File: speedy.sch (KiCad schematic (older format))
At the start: 22 parts

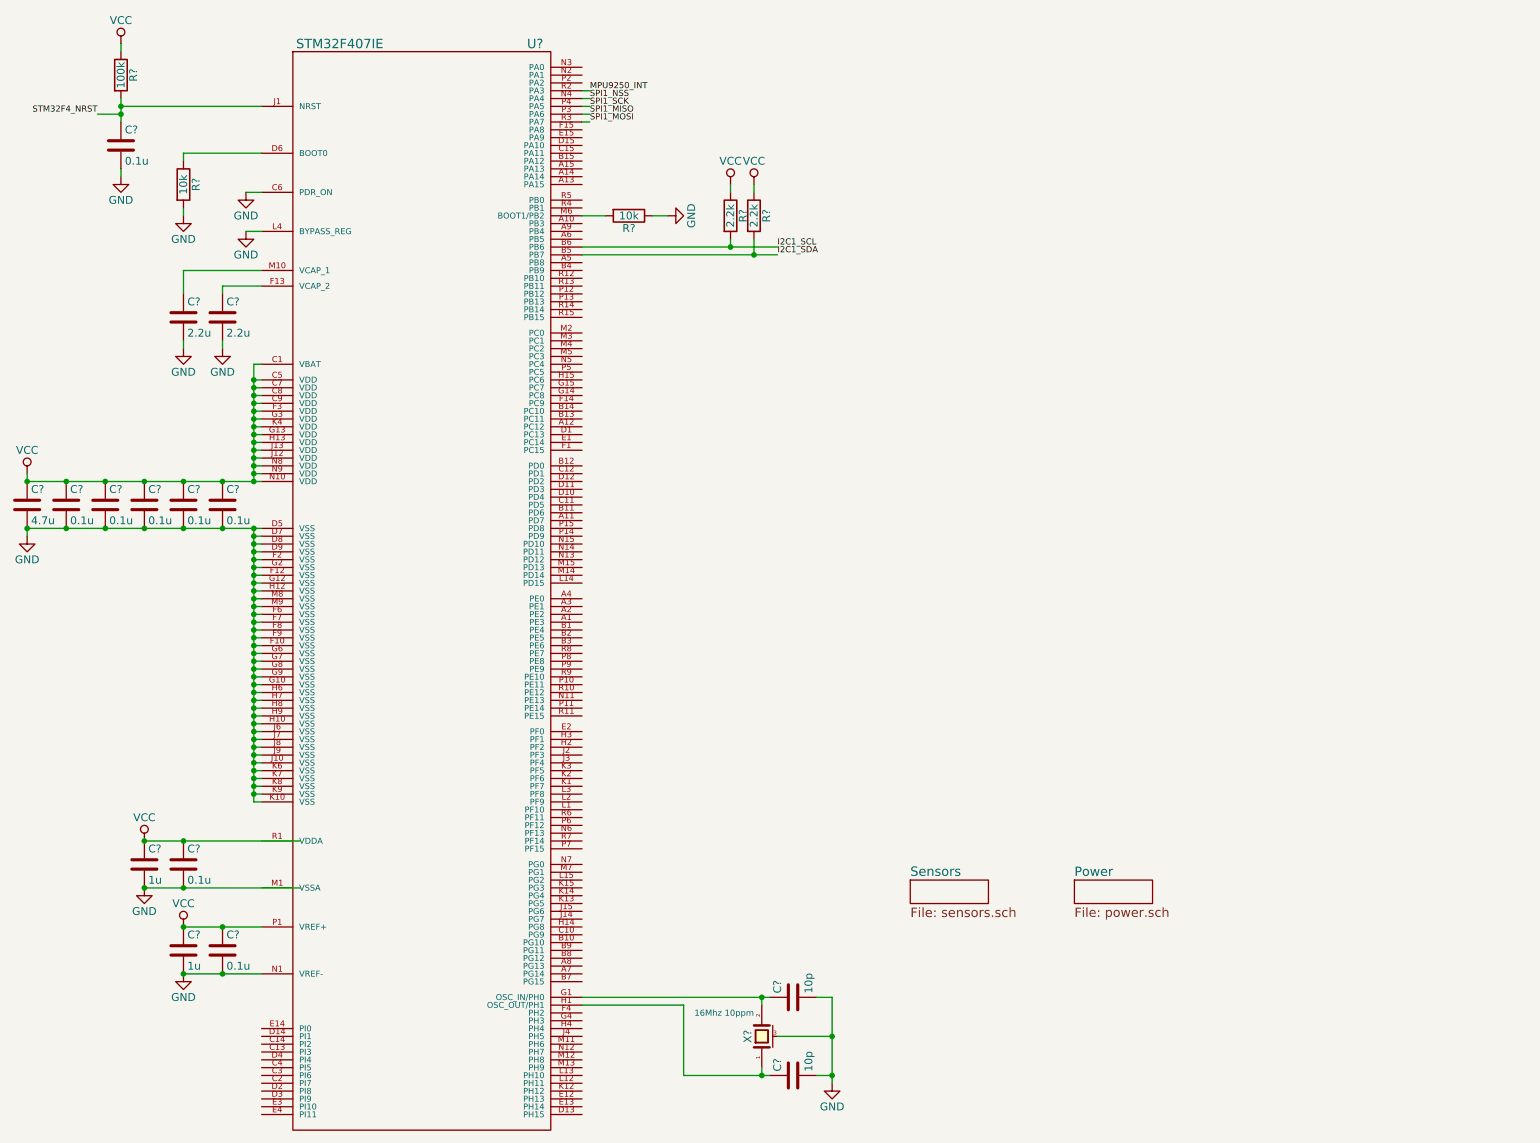
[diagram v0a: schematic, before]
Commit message: LiPo recharge circuit
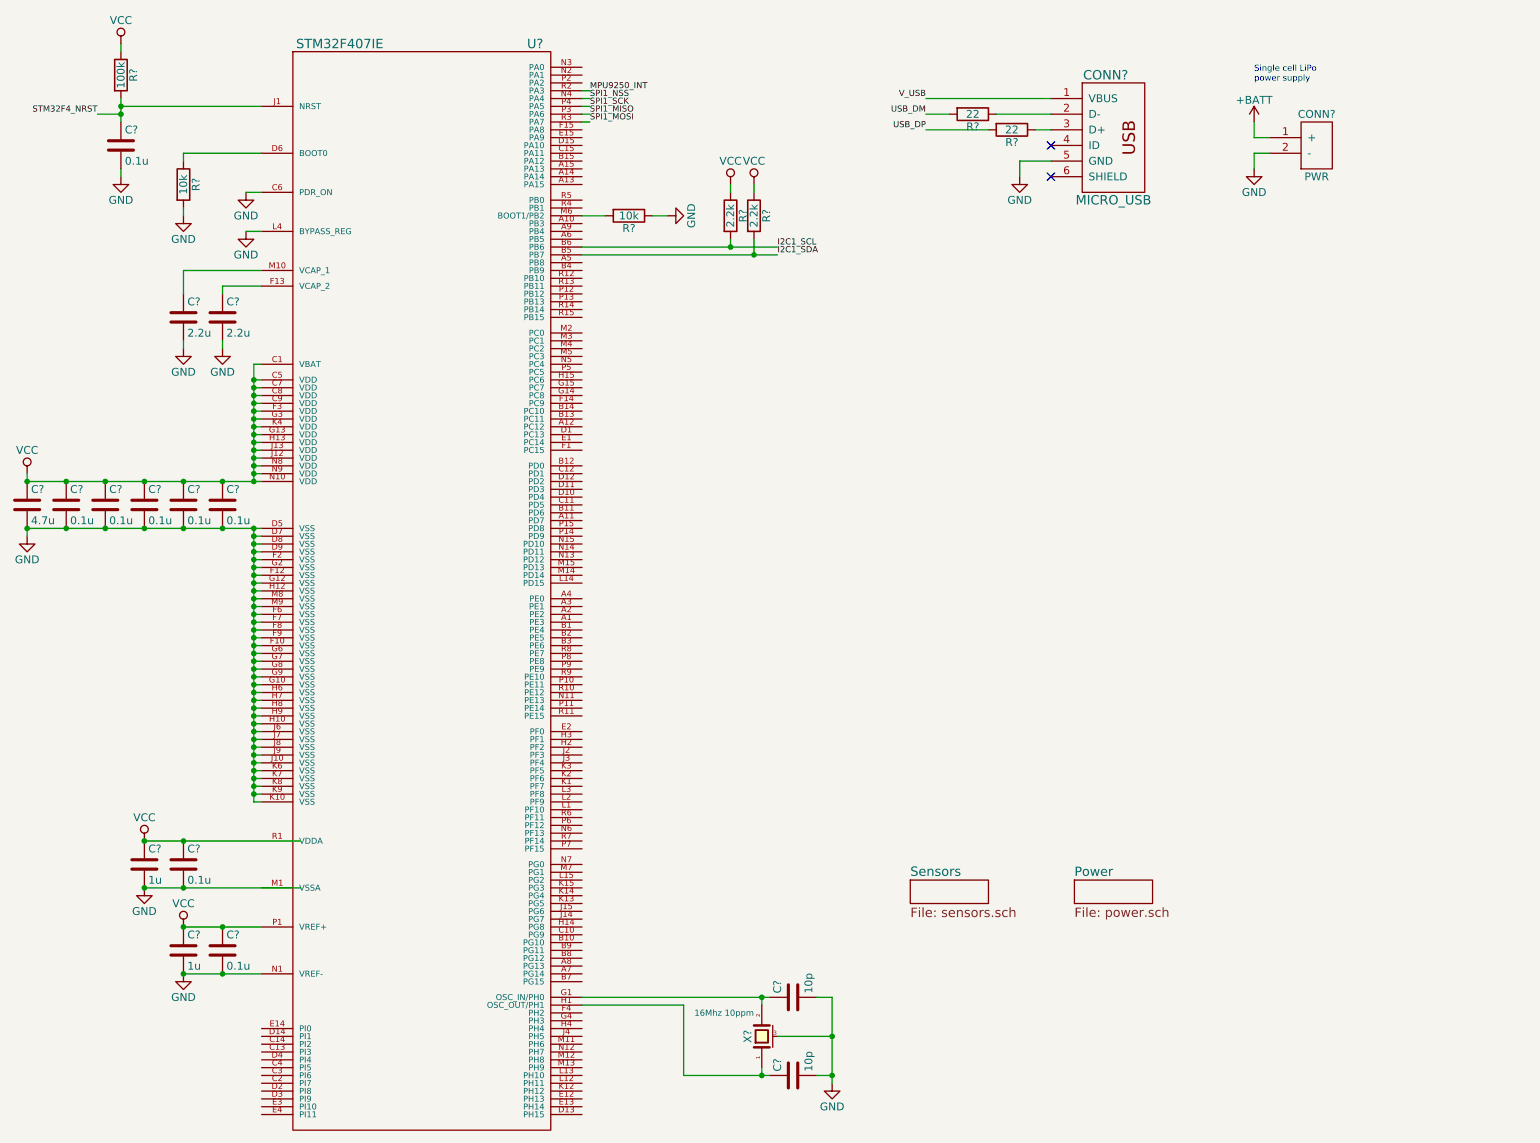
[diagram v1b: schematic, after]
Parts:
- added CONN?: MICRO_USB, symbol MICRO_USB
- added CONN?: PWR, MODULE, symbol PWR
- added R? (x2): 22, symbol R
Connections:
- net GND: now also CONN?.2 (-), CONN?.5 (GND), CONN?.MECH (GND)
- new net: CONN?.2 (D-), R?.1
- new net: CONN?.3 (D+), R?.1
- new net +BATT: CONN?.1 (+)
- new net USB_DM: R?.2
- new net USB_DP: R?.2
- new net V_USB: CONN?.1 (VBUS)
- no-connect marks 0 -> 2
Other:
- note added: "Single cell LiPo \npower supply\n"

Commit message: Update schematic labels to handle hierarchical signal dependencies
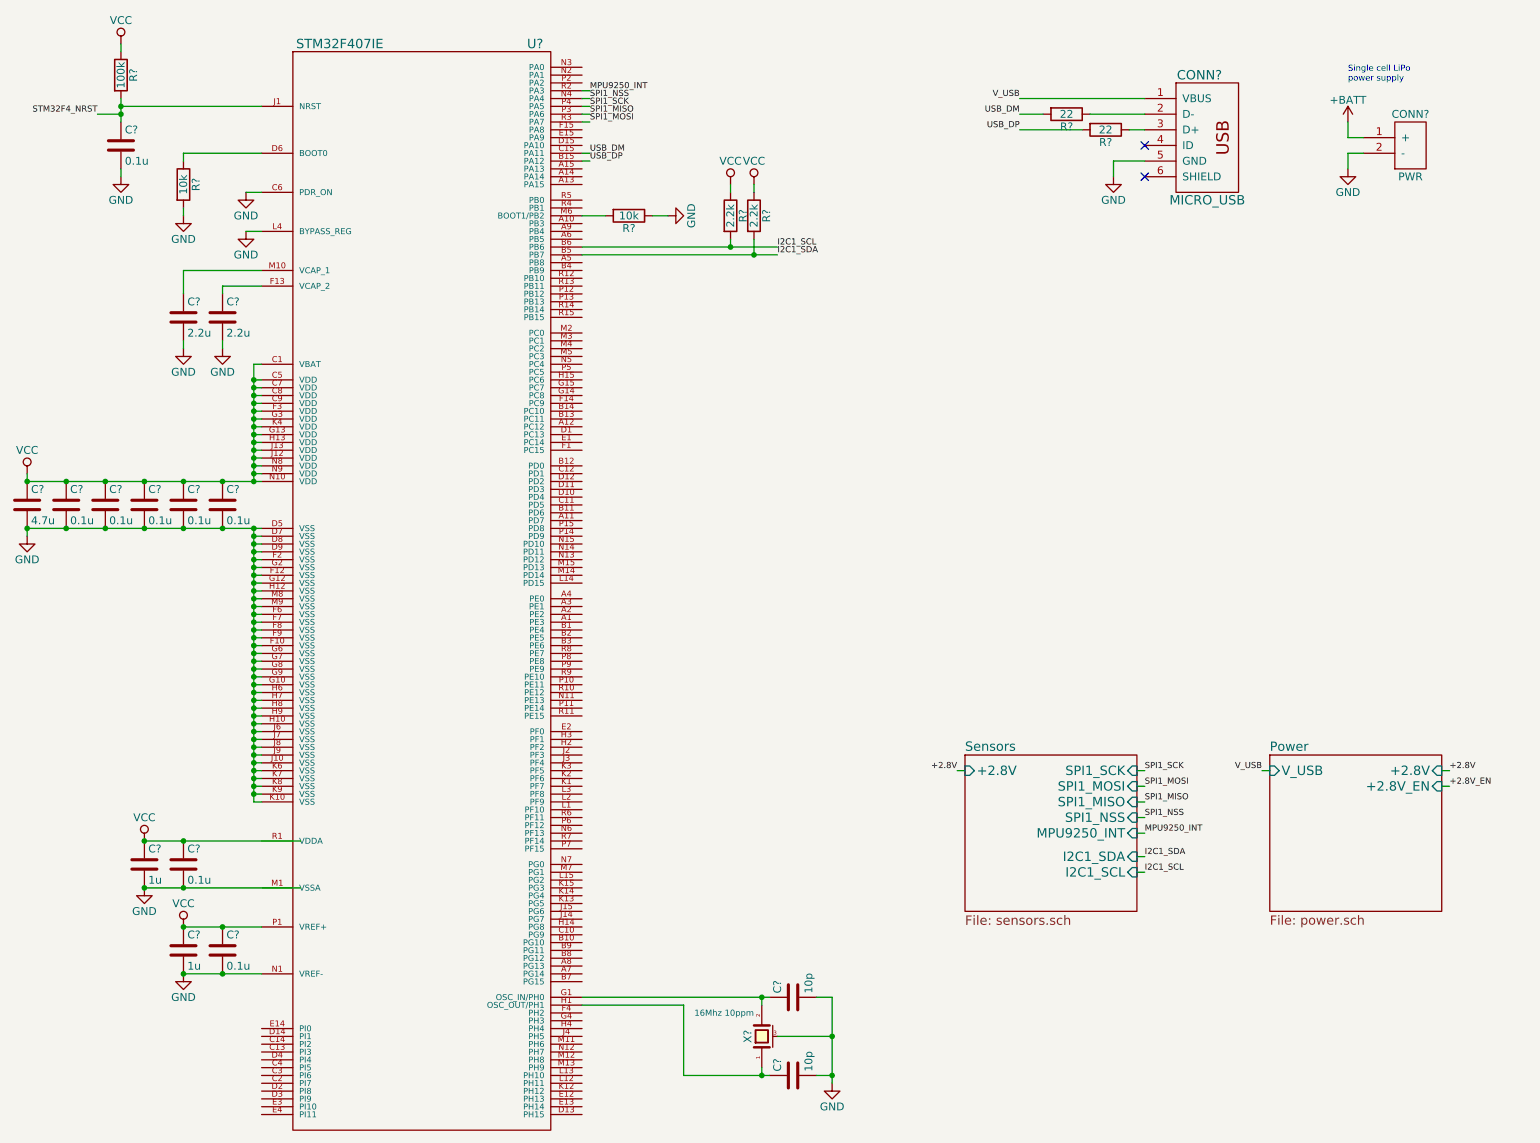
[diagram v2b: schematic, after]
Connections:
- net USB_DM: now also U?.C15 (PA11)
- net USB_DP: now also U?.B15 (PA12)
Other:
- moved on the sheet: CONN?, R?

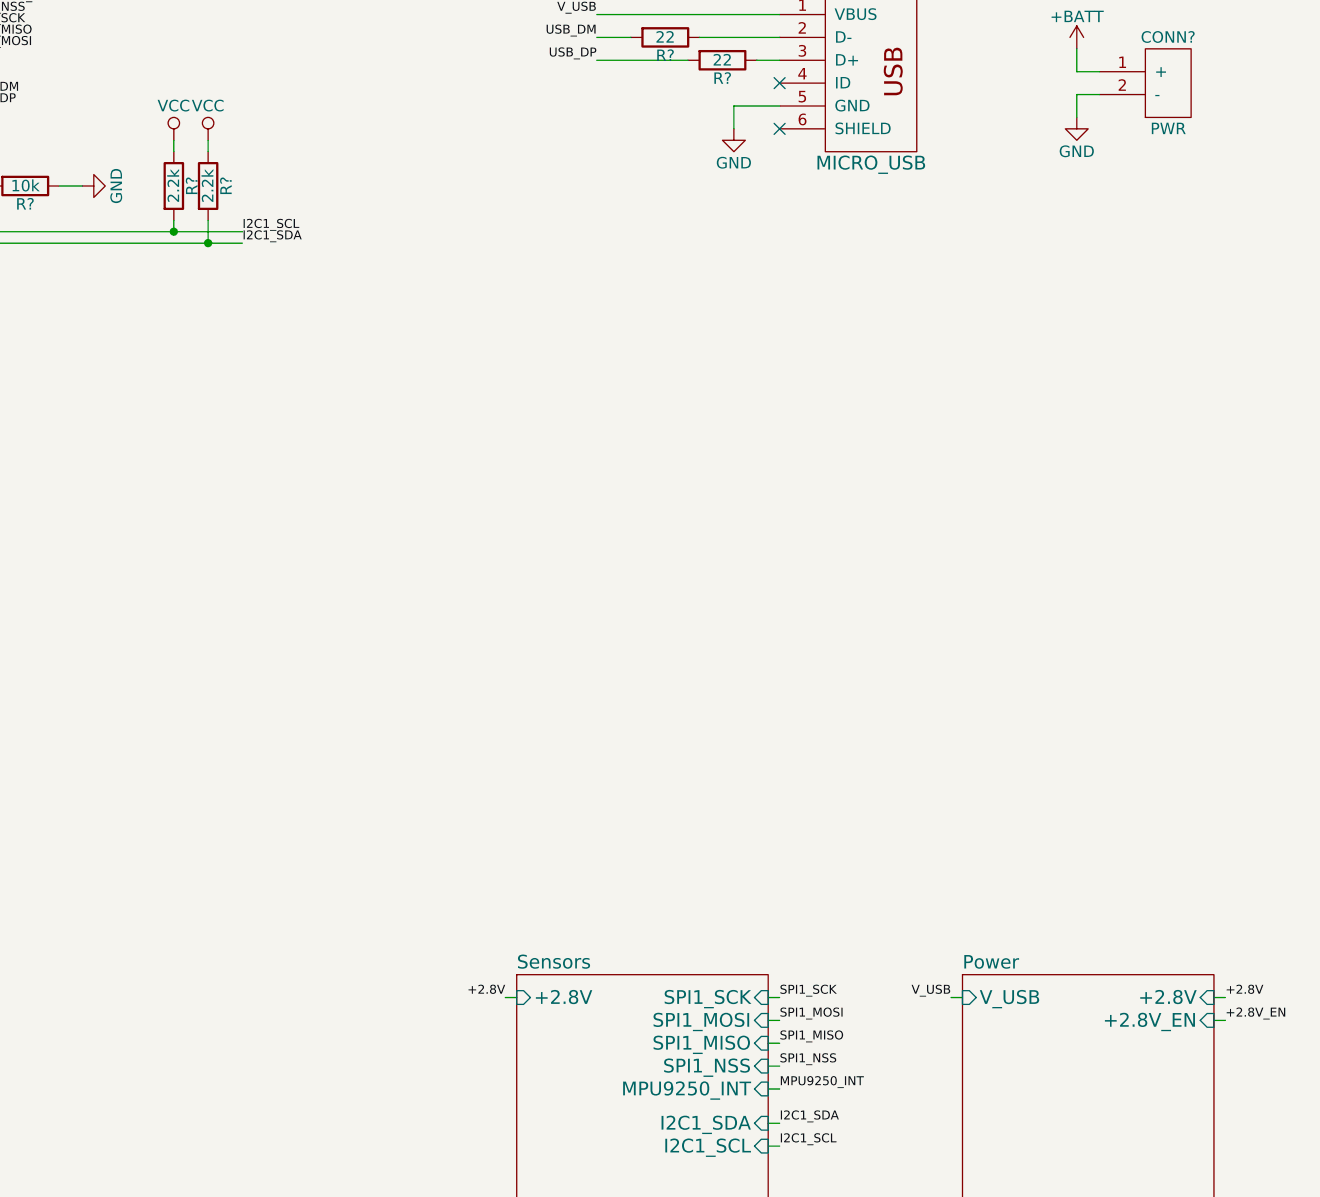
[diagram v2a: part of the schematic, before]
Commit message: Add principal power supply
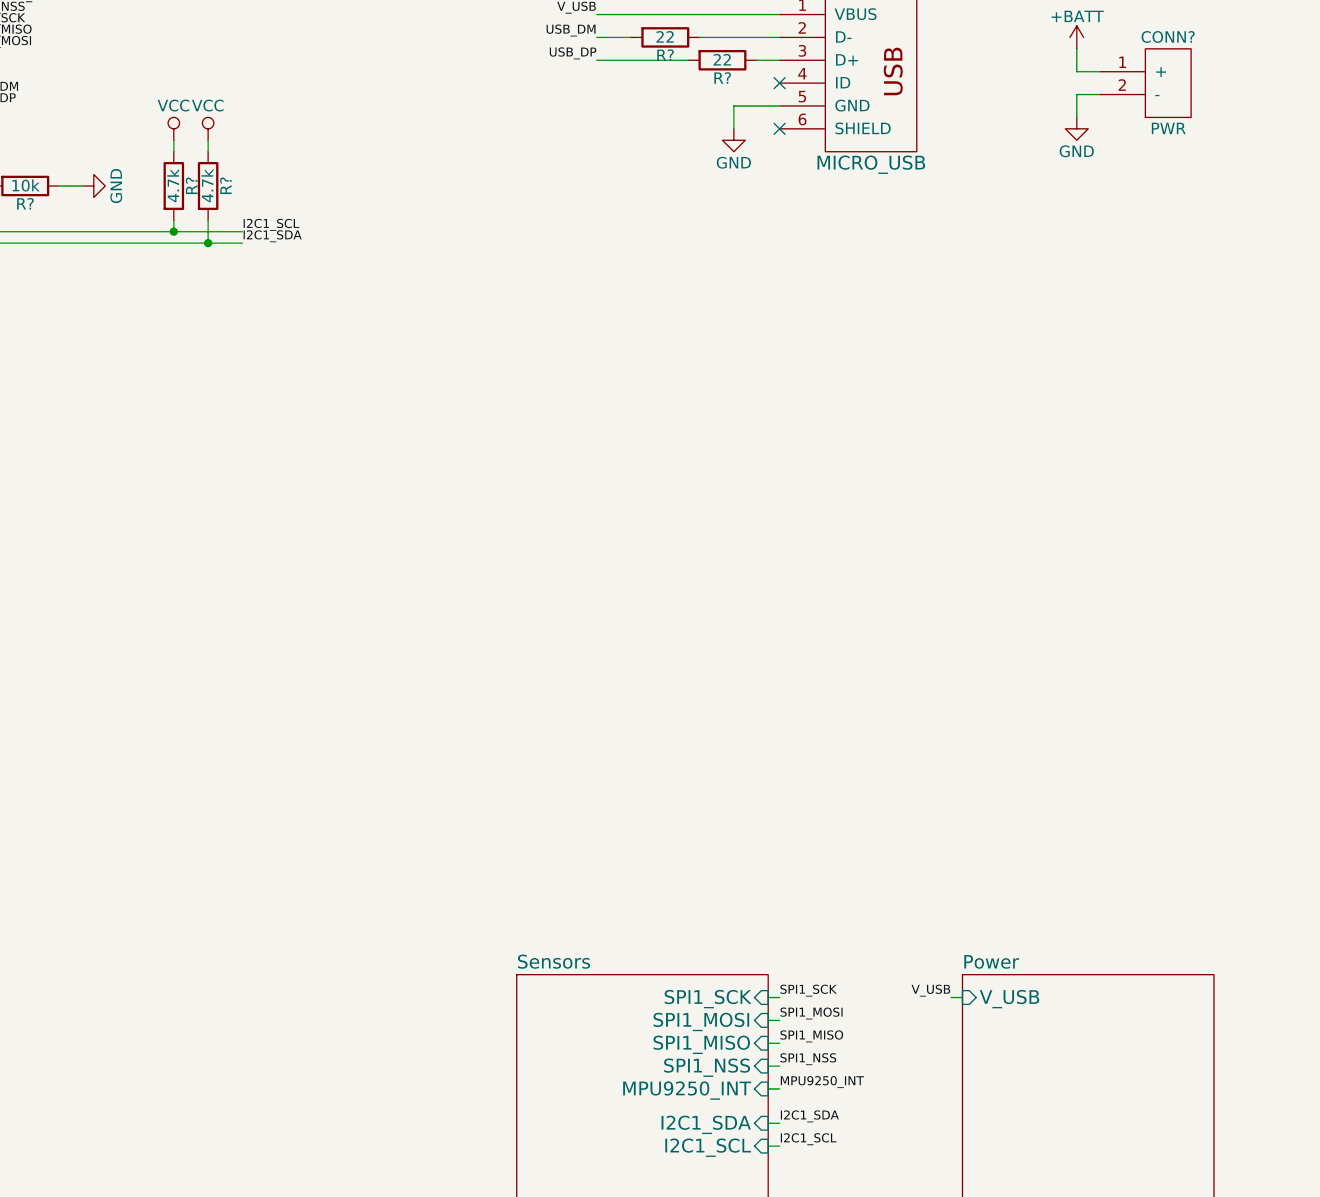
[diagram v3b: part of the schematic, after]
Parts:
- R? (x2): value 2.2k -> 4.7k
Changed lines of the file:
@@
 F5 "SPI1_NSS" I R 8450 5650 60
 F6 "MPU9250_INT" I R 8450 5750 60
-F7 "+2.8V" I L 7350 5350 60
-F8 "I2C1_SDA" I R 8450 5900 60
-F9 "I2C1_SCL" I R 8450 6000 60
+F7 "I2C1_SDA" I R 8450 5900 60
+F8 "I2C1_SCL" I R 8450 6000 60
 $EndSheet
 Text Label 4950 1050 0    39   ~ 0
@@
 P 5850 1800
 F 0 "R?" V 5930 1800 50  0000 C CNN
-F 1 "2.2k" V 5850 1800 50  0000 C CNN
+F 1 "4.7k" V 5850 1800 50  0000 C CNN
 F 2 "" V 5780 1800 30  0000 C CNN
 F 3 "" H 5850 1800 30  0000 C CNN
@@
 P 6000 1800
 F 0 "R?" V 6080 1800 50  0000 C CNN
-F 1 "2.2k" V 6000 1800 50  0000 C CNN
+F 1 "4.7k" V 6000 1800 50  0000 C CNN
 F 2 "" V 5930 1800 30  0000 C CNN
 F 3 "" H 6000 1800 30  0000 C CNN
@@
 	1    0    0    -1
 $EndComp
-$Sheet
-S 9300 5250 1100 1000
-U 55379F3E
-F0 "Power" 59
-F1 "power.sch" 59
-F2 "V_USB" I L 9300 5350 60
-F3 "+2.8V_EN" I R 10400 5450 60
-F4 "+2.8V" I R 10400 5350 60
-$EndSheet
 $Comp
 L MICRO_USB CONN?
@@
 Text Label 8500 5750 0    39   ~ 0
 MPU9250_INT
-Text Label 7300 5350 2    39   ~ 0
-+2.8V
-Text Label 10450 5350 0    39   ~ 0
-+2.8V
-Text Label 10450 5450 0    39   ~ 0
-+2.8V_EN
 Text Label 9250 5350 2    39   ~ 0
 V_USB
@@
 	9800 1400 9900 1400
 Wire Wire Line
-	7300 5350 7350 5350
-Wire Wire Line
 	8500 5350 8450 5350
 Wire Wire Line
@@
 	8450 6000 8500 6000
 Wire Wire Line
-	10450 5350 10400 5350
-Wire Wire Line
-	10450 5450 10400 5450
-Wire Wire Line
 	9250 5350 9300 5350
 Wire Wire Line
@@
 Wire Wire Line
 	4900 1400 4950 1400
+$Sheet
+S 9300 5250 1100 1000
+U 55379F3E
+F0 "Power" 59
+F1 "power.sch" 59
+F2 "V_USB" I L 9300 5350 60
+$EndSheet
 $EndSCHEMATC
